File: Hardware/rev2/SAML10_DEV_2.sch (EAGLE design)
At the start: 18 parts, among them J1 CORTEX_DEBUG_PTH, Y1 32.768kHz

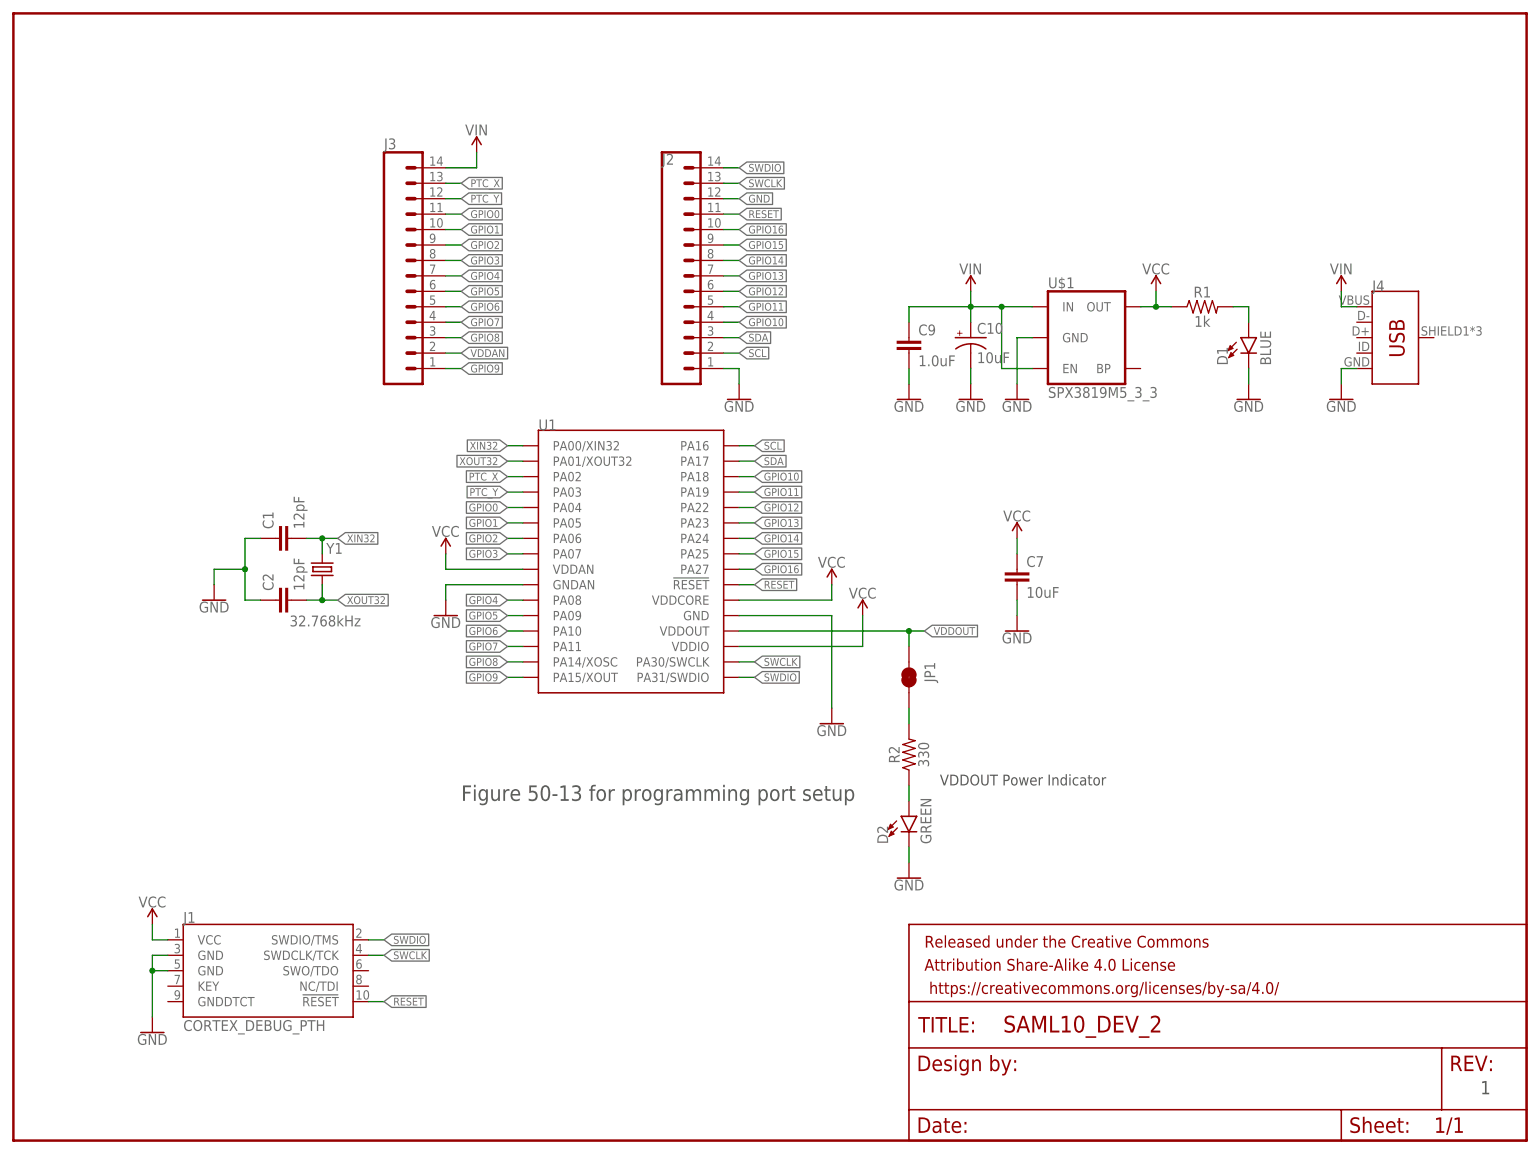
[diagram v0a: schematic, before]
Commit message: power pins fixed, added reset switch
RESET active LOW, pulled RESET High by default
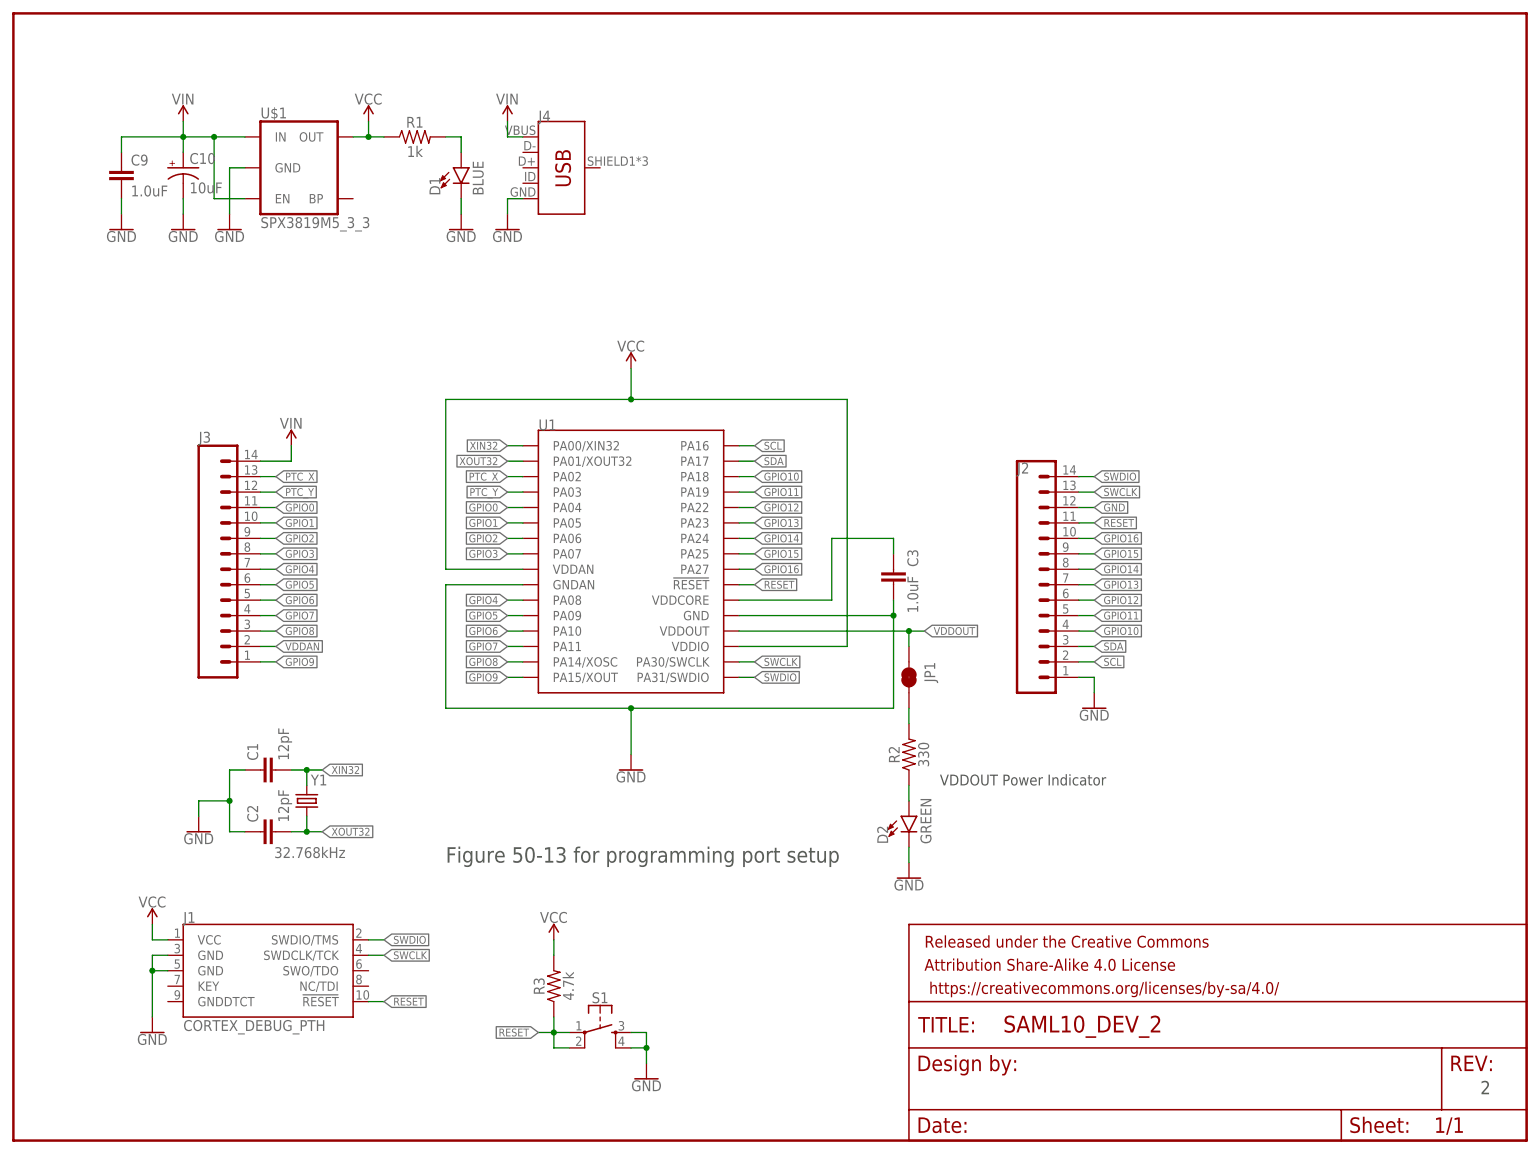
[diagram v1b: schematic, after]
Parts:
- removed C7: 10uF, SparkFun-Capacitors:10UF-0603-6.3V-20%
- added C3: 1.0uF, SparkFun-Capacitors:1.0UF-0603-16V-10%
- added R3: 4.7k, SparkFun-Resistors:4.7KOHM-0603-1/10W-1%
- added S1: (no value), SparkFun-Switches:MOMENTARY-SWITCH-SPST-2-SMD-4.6X2.8MM
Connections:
- new net N$3: C3.1, U1.VDDCORE
- net GND: now also C3.2, S1.3, S1.4; no longer C7.2
- net RESET: now also R3.1, S1.1, S1.2
- net VCC: now also R3.2; no longer C7.1, U1.VDDCORE
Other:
- note added: "2"
- note removed: "1"
- moved on the sheet: C1, C10, C2, C9, D1, J2, J3, J4, R1, U$1, Y1
